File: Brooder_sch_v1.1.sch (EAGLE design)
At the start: 32 parts, among them J1 DCJ0202, J2 1X2-3.5MM, U1 328P

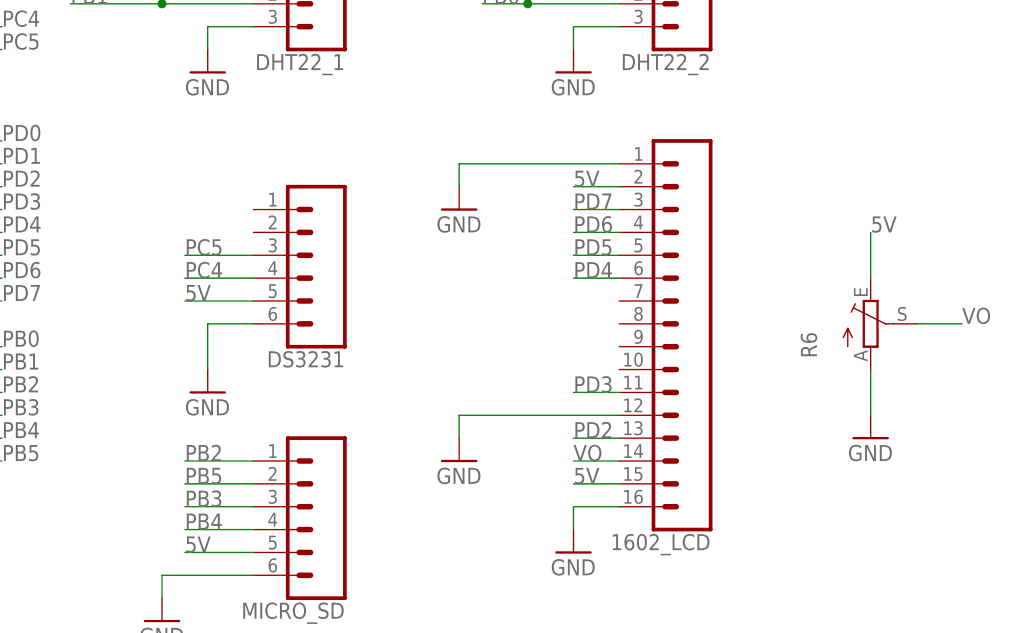
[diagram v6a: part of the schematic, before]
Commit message: Resolves inconsistencies between the board and schematic
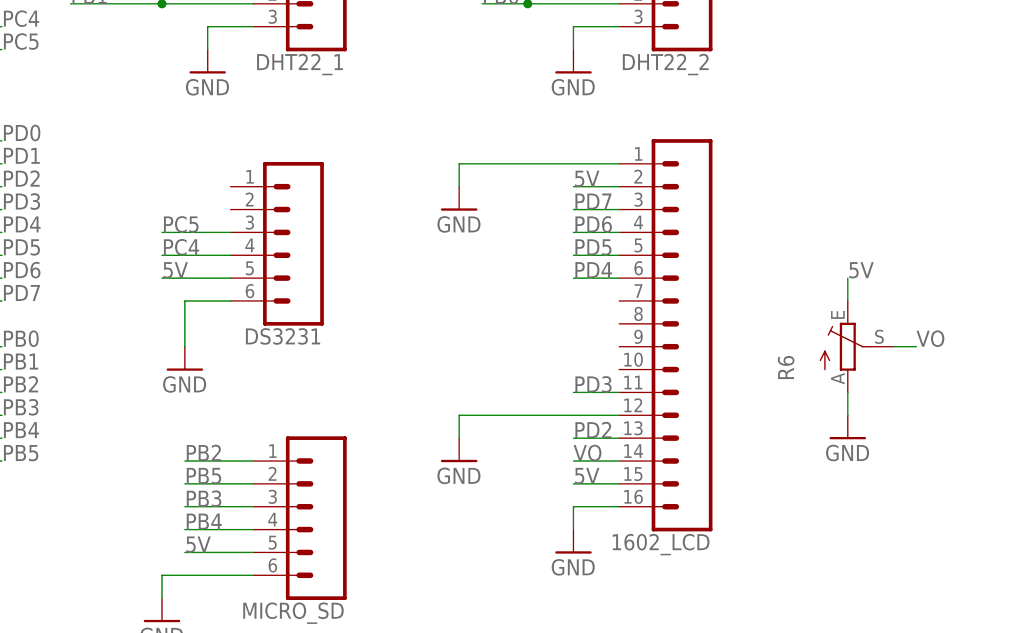
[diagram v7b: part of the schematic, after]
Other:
- moved on the sheet: DS3231, R6
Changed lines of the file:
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@@
 <part name="GND18" library="supply1" library_urn="urn:adsk.eagle:library:371" deviceset="GND" device=""/>
 <part name="J2" library="adafruit" deviceset="1X2" device="-3.5MM"/>
-<part name="DS3231" library="SparkFun-Connectors" deviceset="CONN_06" device="NO_SILK_FEMALE_PTH"/>
-<part name="GND24" library="supply1" library_urn="urn:adsk.eagle:library:371" deviceset="GND" device=""/>
 <part name="R5" library="SparkFun-Resistors" deviceset="10MOHM" device="-HORIZ-1/4W-5%" value="220"/>
 <part name="TEST_LED" library="adafruit" deviceset="LED" device="5MM"/>
+<part name="GND16" library="supply1" library_urn="urn:adsk.eagle:library:371" deviceset="GND" device=""/>
+<part name="R6" library="pot" library_urn="urn:adsk.eagle:library:331" deviceset="TRIM_EU-" device="RJ6" package3d_urn="urn:adsk.eagle:package:22699/1"/>
+<part name="GND24" library="supply1" library_urn="urn:adsk.eagle:library:371" deviceset="GND" device=""/>
+<part name="DS3231" library="SparkFun-Connectors" deviceset="CONN_06" device="NO_SILK_FEMALE_PTH"/>
 <part name="GND25" library="supply1" library_urn="urn:adsk.eagle:library:371" deviceset="GND" device=""/>
-<part name="R6" library="pot" library_urn="urn:adsk.eagle:library:331" deviceset="TRIM_EU-" device="RJ6" package3d_urn="urn:adsk.eagle:package:22699/1"/>
-<part name="GND26" library="supply1" library_urn="urn:adsk.eagle:library:371" deviceset="GND" device=""/>
 </parts>
 <sheets>
@@
 </instance>
 <instance part="J2" gate="G$1" x="-55.88" y="121.92" rot="R90"/>
-<instance part="DS3231" gate="G$1" x="116.84" y="68.58" smashed="yes" rot="R180">
-<attribute name="VALUE" x="121.92" y="78.486" size="1.778" layer="96" font="vector" rot="R180"/>
-<attribute name="NAME" x="121.92" y="57.912" size="1.778" layer="95" font="vector" rot="R180"/>
-</instance>
-<instance part="GND24" gate="1" x="106.68" y="53.34" smashed="yes">
-<attribute name="VALUE" x="104.14" y="50.8" size="1.778" layer="96"/>
-</instance>
 <instance part="R5" gate="G$1" x="104.14" y="15.24" smashed="yes" rot="R180">
 <attribute name="NAME" x="104.14" y="13.716" size="1.778" layer="95" font="vector" rot="R180" align="bottom-center"/>
@@
 <attribute name="VALUE" x="118.872" y="20.955" size="1.778" layer="96" rot="R180"/>
 </instance>
-<instance part="GND25" gate="1" x="124.46" y="12.7" smashed="yes">
+<instance part="GND16" gate="1" x="124.46" y="12.7" smashed="yes">
 <attribute name="VALUE" x="121.92" y="10.16" size="1.778" layer="96"/>
 </instance>
-<instance part="R6" gate="1" x="180.34" y="60.96"/>
-<instance part="GND26" gate="1" x="180.34" y="48.26" smashed="yes">
-<attribute name="VALUE" x="177.8" y="45.72" size="1.778" layer="96"/>
+<instance part="R6" gate="1" x="177.8" y="58.42"/>
+<instance part="GND24" gate="1" x="177.8" y="48.26" smashed="yes">
+<attribute name="VALUE" x="175.26" y="45.72" size="1.778" layer="96"/>
+</instance>
+<instance part="DS3231" gate="G$1" x="114.3" y="71.12" smashed="yes" rot="R180">
+<attribute name="VALUE" x="119.38" y="81.026" size="1.778" layer="96" font="vector" rot="R180"/>
+<attribute name="NAME" x="119.38" y="60.452" size="1.778" layer="95" font="vector" rot="R180"/>
+</instance>
+<instance part="GND25" gate="1" x="104.14" y="55.88" smashed="yes">
+<attribute name="VALUE" x="101.6" y="53.34" size="1.778" layer="96"/>
 </instance>
 </instances>
@@
 </segment>
 <segment>
+<pinref part="TEST_LED" gate="G$1" pin="C"/>
+<pinref part="GND16" gate="1" pin="GND"/>
+<wire x1="119.38" y1="15.24" x2="124.46" y2="15.24" width="0.1524" layer="91"/>
+</segment>
+<segment>
+<pinref part="R6" gate="1" pin="A"/>
+<wire x1="177.8" y1="53.34" x2="177.8" y2="50.8" width="0.1524" layer="91"/>
+<pinref part="GND24" gate="1" pin="GND"/>
+</segment>
+<segment>
 <pinref part="DS3231" gate="G$1" pin="6"/>
-<wire x1="111.76" y1="60.96" x2="106.68" y2="60.96" width="0.1524" layer="91"/>
-<wire x1="106.68" y1="60.96" x2="106.68" y2="55.88" width="0.1524" layer="91"/>
-<pinref part="GND24" gate="1" pin="GND"/>
-</segment>
-<segment>
-<pinref part="TEST_LED" gate="G$1" pin="C"/>
+<wire x1="109.22" y1="63.5" x2="104.14" y2="63.5" width="0.1524" layer="91"/>
+<wire x1="104.14" y1="63.5" x2="104.14" y2="58.42" width="0.1524" layer="91"/>
 <pinref part="GND25" gate="1" pin="GND"/>
-<wire x1="119.38" y1="15.24" x2="124.46" y2="15.24" width="0.1524" layer="91"/>
-</segment>
-<segment>
-<pinref part="R6" gate="1" pin="A"/>
-<wire x1="180.34" y1="55.88" x2="180.34" y2="50.8" width="0.1524" layer="91"/>
-<pinref part="GND26" gate="1" pin="GND"/>
 </segment>
 </net>
@@
 </segment>
 <segment>
+<pinref part="R6" gate="1" pin="E"/>
+<wire x1="177.8" y1="63.5" x2="177.8" y2="66.04" width="0.1524" layer="91"/>
+<label x="177.8" y="66.04" size="1.778" layer="95"/>
+</segment>
+<segment>
 <pinref part="DS3231" gate="G$1" pin="5"/>
-<wire x1="111.76" y1="63.5" x2="104.14" y2="63.5" width="0.1524" layer="91"/>
-<label x="104.14" y="63.5" size="1.778" layer="95"/>
-</segment>
-<segment>
-<pinref part="R6" gate="1" pin="E"/>
-<wire x1="180.34" y1="66.04" x2="180.34" y2="71.12" width="0.1524" layer="91"/>
-<label x="180.34" y="71.12" size="1.778" layer="95"/>
+<wire x1="109.22" y1="66.04" x2="101.6" y2="66.04" width="0.1524" layer="91"/>
+<label x="101.6" y="66.04" size="1.778" layer="95"/>
 </segment>
 </net>
@@
 <segment>
 <pinref part="R6" gate="1" pin="S"/>
-<wire x1="185.42" y1="60.96" x2="190.5" y2="60.96" width="0.1524" layer="91"/>
-<label x="190.5" y="60.96" size="1.778" layer="95"/>
+<wire x1="182.88" y1="58.42" x2="185.42" y2="58.42" width="0.1524" layer="91"/>
+<label x="185.42" y="58.42" size="1.778" layer="95"/>
 </segment>
 </net>
@@
 </segment>
 </net>
+<net name="N$1" class="0">
+<segment>
+<pinref part="R5" gate="G$1" pin="1"/>
+<pinref part="TEST_LED" gate="G$1" pin="A"/>
+<wire x1="109.22" y1="15.24" x2="111.76" y2="15.24" width="0.1524" layer="91"/>
+</segment>
+</net>
+<net name="PC1" class="0">
+<segment>
+<pinref part="U1" gate="U1" pin="PC1(ADC1)"/>
+<wire x1="76.2" y1="101.6" x2="83.82" y2="101.6" width="0.1524" layer="91"/>
+<label x="83.82" y="101.6" size="1.778" layer="95"/>
+</segment>
+<segment>
+<pinref part="R5" gate="G$1" pin="2"/>
+<wire x1="99.06" y1="15.24" x2="93.98" y2="15.24" width="0.1524" layer="91"/>
+<label x="93.98" y="15.24" size="1.778" layer="95"/>
+</segment>
+</net>
 <net name="PC4" class="0">
 <segment>
 <pinref part="DS3231" gate="G$1" pin="4"/>
-<wire x1="111.76" y1="66.04" x2="104.14" y2="66.04" width="0.1524" layer="91"/>
-<label x="104.14" y="66.04" size="1.778" layer="95"/>
+<wire x1="109.22" y1="68.58" x2="101.6" y2="68.58" width="0.1524" layer="91"/>
+<label x="101.6" y="68.58" size="1.778" layer="95"/>
 </segment>
 <segment>
@@
 <segment>
 <pinref part="DS3231" gate="G$1" pin="3"/>
-<wire x1="111.76" y1="68.58" x2="104.14" y2="68.58" width="0.1524" layer="91"/>
-<label x="104.14" y="68.58" size="1.778" layer="95"/>
+<wire x1="109.22" y1="71.12" x2="101.6" y2="71.12" width="0.1524" layer="91"/>
+<label x="101.6" y="71.12" size="1.778" layer="95"/>
 </segment>
 <segment>
@@
 </segment>
 </net>
-<net name="N$1" class="0">
-<segment>
-<pinref part="R5" gate="G$1" pin="1"/>
-<pinref part="TEST_LED" gate="G$1" pin="A"/>
-<wire x1="109.22" y1="15.24" x2="111.76" y2="15.24" width="0.1524" layer="91"/>
-</segment>
-</net>
-<net name="PC1" class="0">
-<segment>
-<pinref part="R5" gate="G$1" pin="2"/>
-<wire x1="99.06" y1="15.24" x2="93.98" y2="15.24" width="0.1524" layer="91"/>
-<label x="93.98" y="15.24" size="1.778" layer="95"/>
-</segment>
-<segment>
-<pinref part="U1" gate="U1" pin="PC1(ADC1)"/>
-<wire x1="76.2" y1="101.6" x2="83.82" y2="101.6" width="0.1524" layer="91"/>
-<label x="83.82" y="101.6" size="1.778" layer="95"/>
-</segment>
-</net>

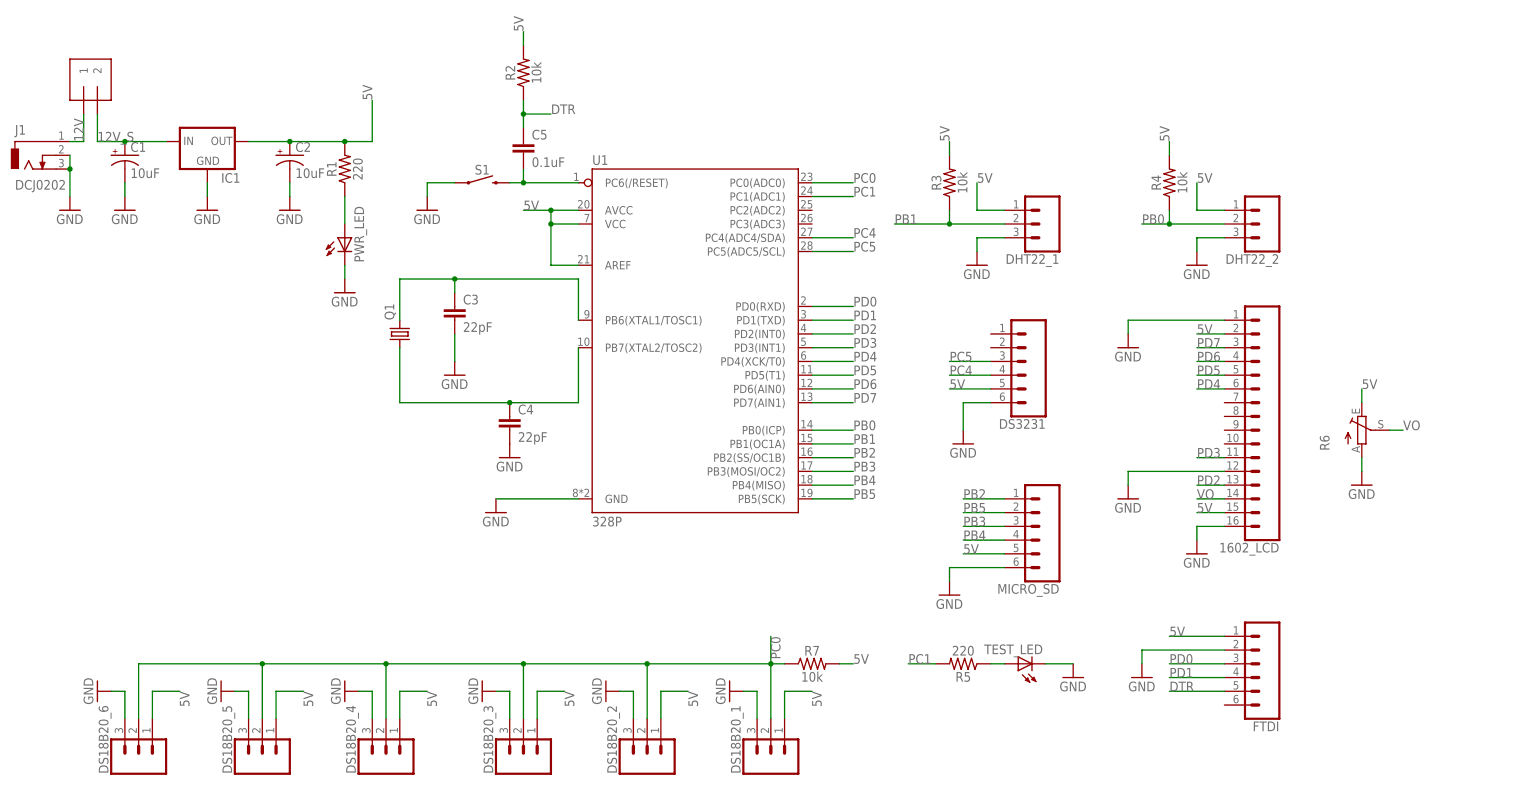
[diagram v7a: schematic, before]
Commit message: Replaces the 7805 eith the lm2596 buck converter
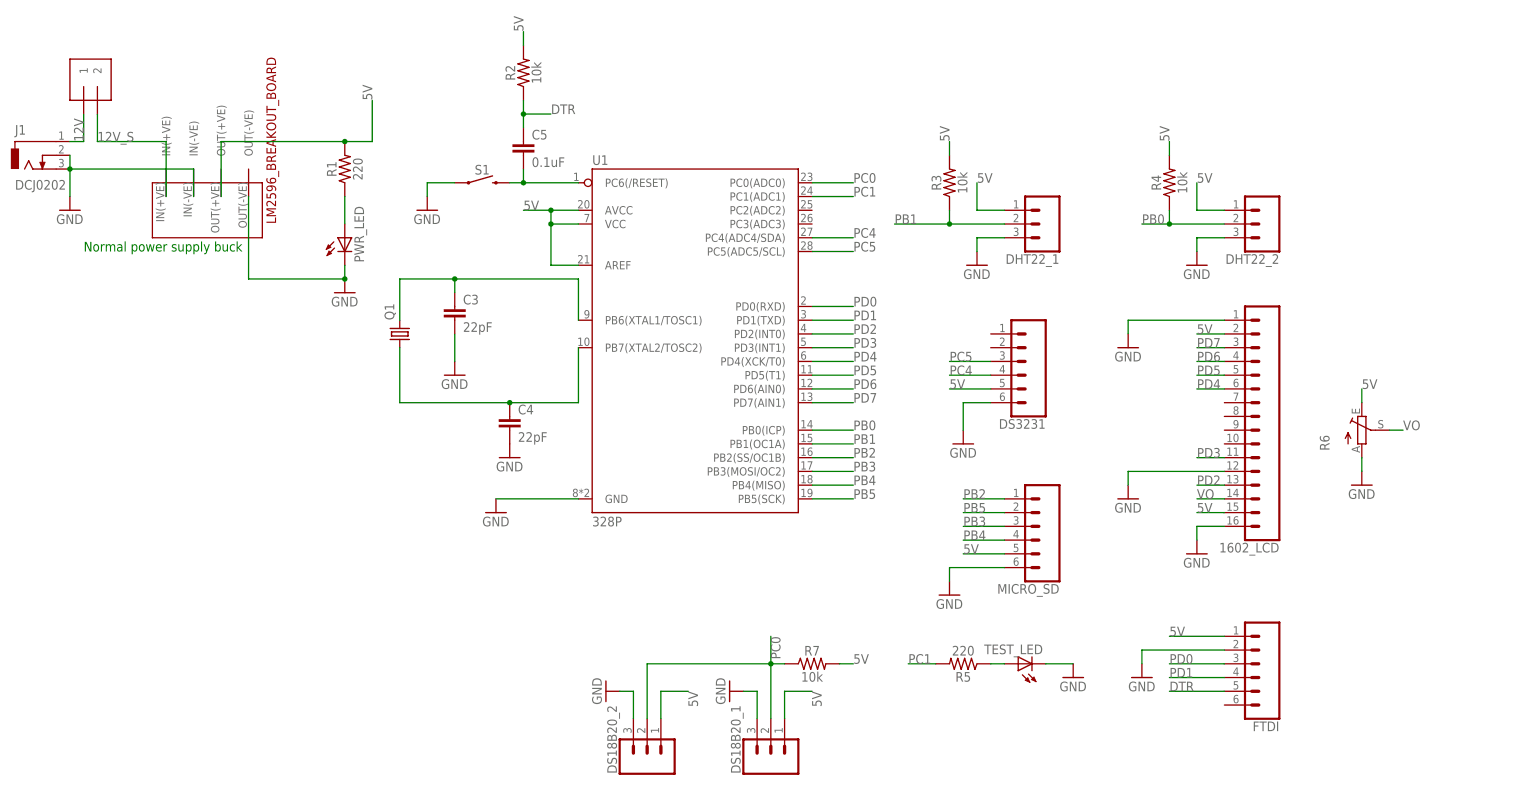
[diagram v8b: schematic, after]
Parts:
- removed C1, C2: 10uF, SparkFun-Capacitors:10UF-POLAR-RADIAL-2.5MM-25V-20%
- removed DS18B20_3, DS18B20_4, DS18B20_5, DS18B20_6: 455-1750-1-ND, SparkFun-Connectors:CONN_03
- removed IC1: (no value), v-reg:78XXS
- added U$2: (no value), LM2596_BREAKOUT_BOARD:LM2596_BREAKOUT_BOARDTHROUGH_HOLE
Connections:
- net 12V_S: now also U$2.IN(+VE); no longer C1.+, IC1.IN
- net 5V: now also U$2.OUT(+VE); no longer C2.+, DS18B20_3.1, DS18B20_4.1, DS18B20_5.1, DS18B20_6.1, IC1.OUT
- net GND: now also U$2.IN(-VE), U$2.OUT(-VE); no longer C1.-, C2.-, DS18B20_3.3, DS18B20_4.3, DS18B20_5.3, DS18B20_6.3, IC1.GND
- net PC0: no longer DS18B20_3.2, DS18B20_4.2, DS18B20_5.2, DS18B20_6.2
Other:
- note added: "Normal power supply buck"
